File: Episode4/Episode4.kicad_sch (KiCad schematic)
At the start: 16 parts, among them J1 BUS 1, J2 BUS 2, J3 BUS 3, J4 BUS 4, J5 BUS 5, J6 BUS 6, J7 BUS 7, J8 Conn_02x31_Top_Bottom, J9 Conn_02x18_Top_Bottom

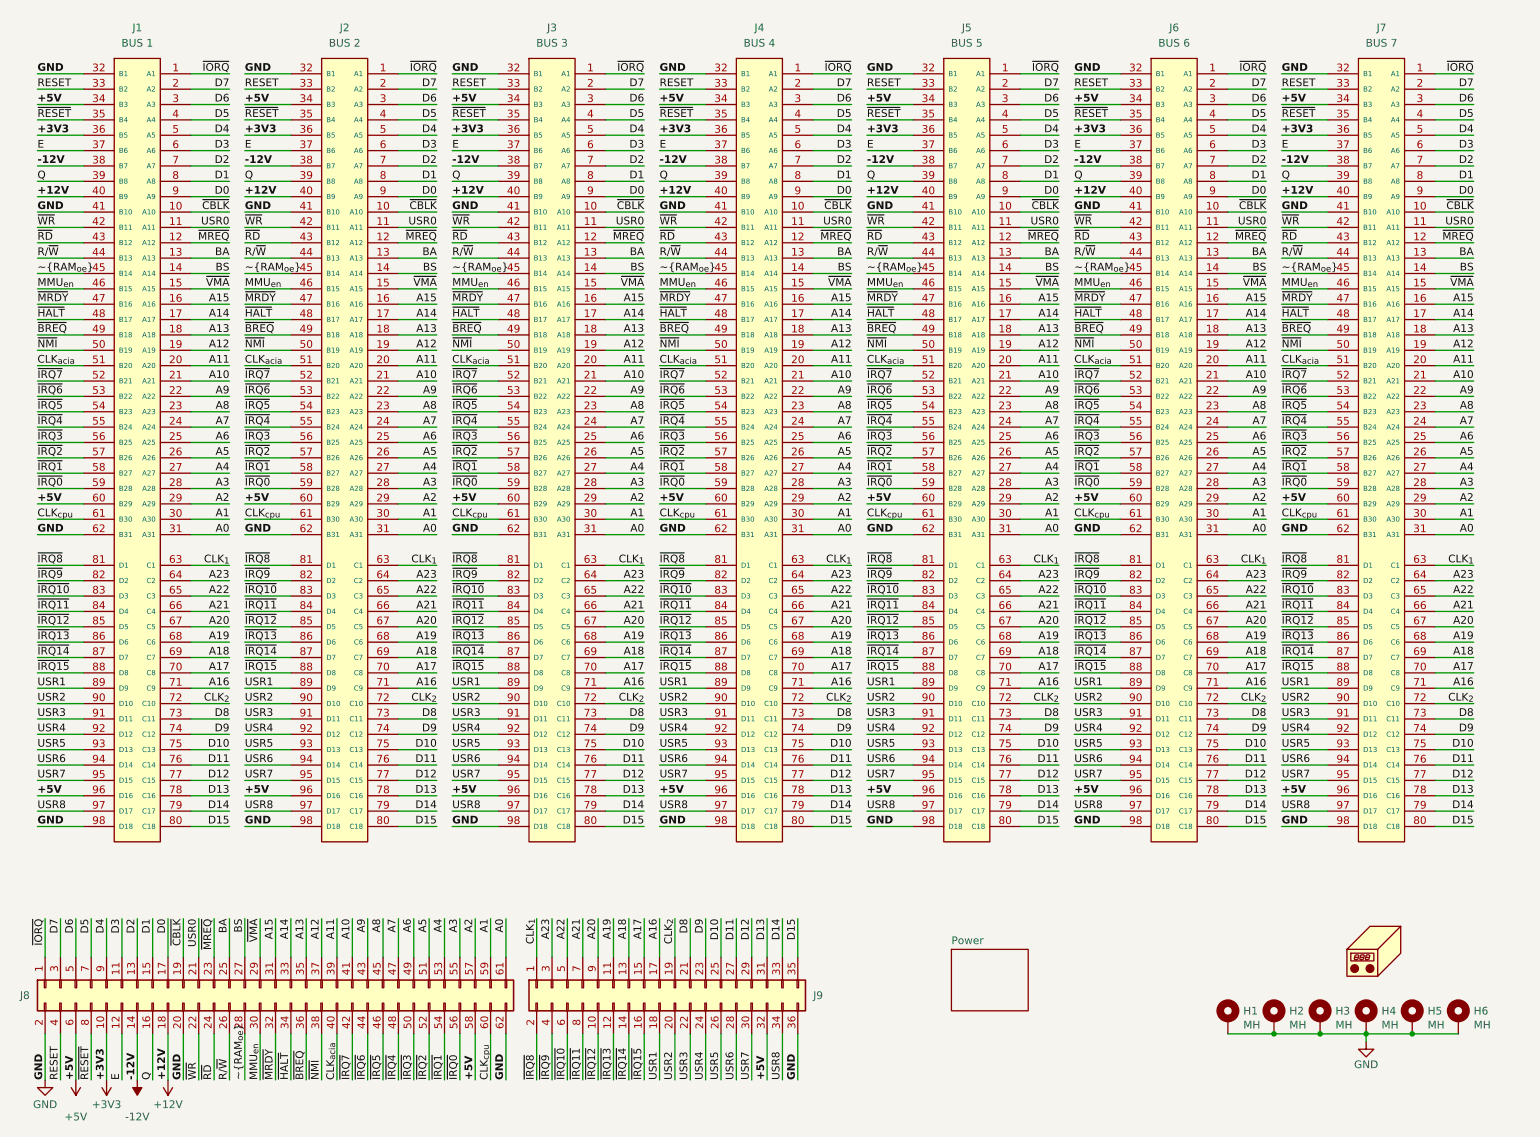
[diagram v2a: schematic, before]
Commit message: Added more capacitors and extended the bus form 7 to 12
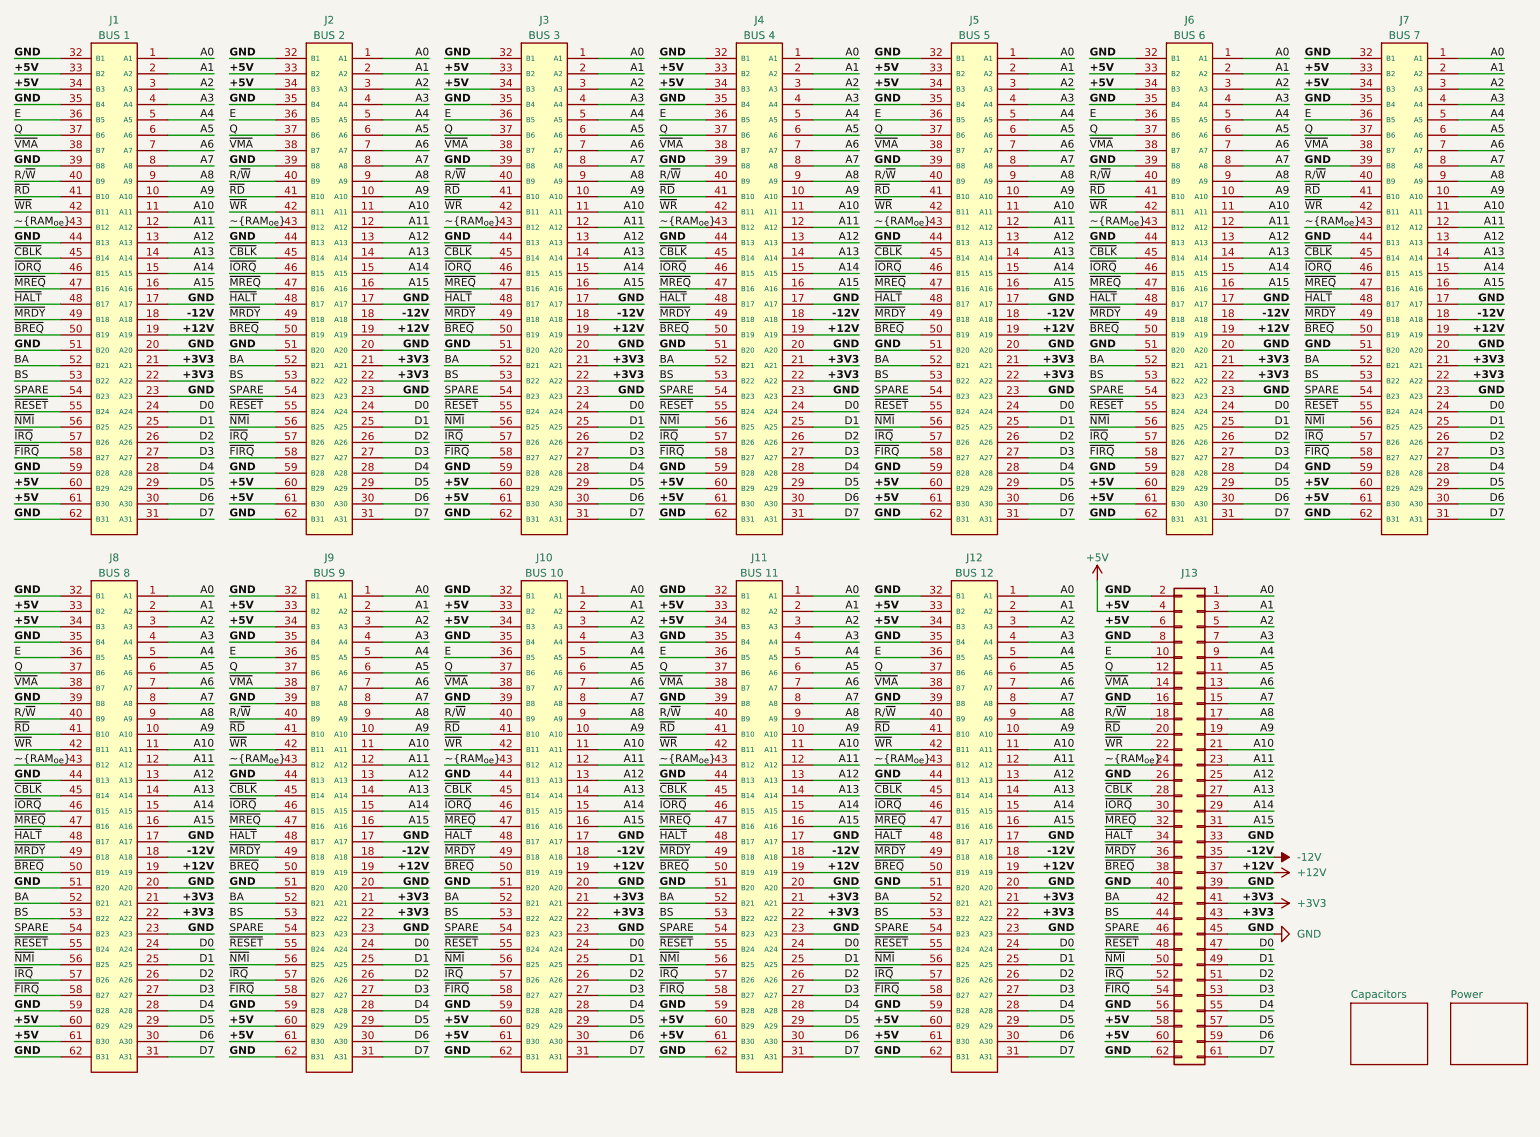
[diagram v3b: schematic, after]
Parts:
- removed H1, H2, H3, H4, H5, H6: MH, MountingHole:MountingHole_3.5mm_Pad_Via, symbol Mechanical:MountingHole_Pad
- removed J1: BUS 1, MicroHobbyist:ISA_Connector_98, symbol MicroHobbyist:ISA_CARD_CONNECTOR_16BIT
- removed J2: BUS 2, MicroHobbyist:ISA_Connector_98, symbol MicroHobbyist:ISA_CARD_CONNECTOR_16BIT
- removed J3: BUS 3, MicroHobbyist:ISA_Connector_98, symbol MicroHobbyist:ISA_CARD_CONNECTOR_16BIT
- removed J4: BUS 4, MicroHobbyist:ISA_Connector_98, symbol MicroHobbyist:ISA_CARD_CONNECTOR_16BIT
- removed J5: BUS 5, MicroHobbyist:ISA_Connector_98, symbol MicroHobbyist:ISA_CARD_CONNECTOR_16BIT
- removed J6: BUS 6, MicroHobbyist:ISA_Connector_98, symbol MicroHobbyist:ISA_CARD_CONNECTOR_16BIT
- removed J7: BUS 7, MicroHobbyist:ISA_Connector_98, symbol MicroHobbyist:ISA_CARD_CONNECTOR_16BIT
- removed J9: Conn_02x18_Top_Bottom, Connector_PinSocket_2.54mm:PinSocket_2x18_P2.54mm_Vertical, symbol Connector_Generic:Conn_02x18_Odd_Even
- removed N1: Housing, MicroHobbyist:ATX_Backplane, symbol Mechanical:Housing
- added J1: BUS 1, MicroHobbyist:ISA_Connector, symbol MicroHobbyist:ISA_CARD_CONNECTOR_8BIT
- added J10: BUS 10, MicroHobbyist:ISA_Connector, symbol MicroHobbyist:ISA_CARD_CONNECTOR_8BIT
- added J11: BUS 11, MicroHobbyist:ISA_Connector, symbol MicroHobbyist:ISA_CARD_CONNECTOR_8BIT
- added J12: BUS 12, MicroHobbyist:ISA_Connector, symbol MicroHobbyist:ISA_CARD_CONNECTOR_8BIT
- added J2: BUS 2, MicroHobbyist:ISA_Connector, symbol MicroHobbyist:ISA_CARD_CONNECTOR_8BIT
- added J3: BUS 3, MicroHobbyist:ISA_Connector, symbol MicroHobbyist:ISA_CARD_CONNECTOR_8BIT
- added J4: BUS 4, MicroHobbyist:ISA_Connector, symbol MicroHobbyist:ISA_CARD_CONNECTOR_8BIT
- added J5: BUS 5, MicroHobbyist:ISA_Connector, symbol MicroHobbyist:ISA_CARD_CONNECTOR_8BIT
- added J6: BUS 6, MicroHobbyist:ISA_Connector, symbol MicroHobbyist:ISA_CARD_CONNECTOR_8BIT
- added J7: BUS 7, MicroHobbyist:ISA_Connector, symbol MicroHobbyist:ISA_CARD_CONNECTOR_8BIT
- added J8: BUS 8, MicroHobbyist:ISA_Connector, symbol MicroHobbyist:ISA_CARD_CONNECTOR_8BIT
- added J9: BUS 9, MicroHobbyist:ISA_Connector, symbol MicroHobbyist:ISA_CARD_CONNECTOR_8BIT
- renumbered J8 to J13
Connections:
- net CLK_{acia} is gone; now on net GND: J13.40 (Pin_40)
- net CLK_{cpu} is gone; now on net +5V: J13.60 (Pin_60)
- net MMU_{en} is gone; now on net ~{IORQ}: J13.30 (Pin_30)
- net RESET is gone; now on net +5V: J13.4 (Pin_4)
- net USR0 is gone; now on net A10: J13.21 (Pin_21)
- net ~{IRQ0} is gone; now on net GND: J13.56 (Pin_56)
- net ~{IRQ3} is gone; now on net ~{NMI}: J13.50 (Pin_50)
- net ~{IRQ4} is gone; now on net ~{RESET}: J13.48 (Pin_48)
- net ~{IRQ6} is gone; now on net BS: J13.44 (Pin_44)
- net ~{IRQ7} is gone; now on net BA: J13.42 (Pin_42)
- net +12V: now also J13.37 (Pin_37), J1.19 (A19), J10.19 (A19), J11.19 (A19), J12.19 (A19), J2.19 (A19), J3.19 (A19), J4.19 (A19), J5.19 (A19), J6.19 (A19), J7.19 (A19), J8.19 (A19), J9.19 (A19); no longer J13.18 (Pin_18)
- net +3V3: now also J13.41 (Pin_41), J13.43 (Pin_43), J1.21 (A21), J1.22 (A22), J10.21 (A21), J10.22 (A22), J11.21 (A21), J11.22 (A22), J12.21 (A21), J12.22 (A22), J2.21 (A21), J2.22 (A22), J3.21 (A21), J3.22 (A22), J4.21 (A21), J4.22 (A22), J5.21 (A21), J5.22 (A22), J6.21 (A21), J6.22 (A22), J7.21 (A21), J7.22 (A22), J8.21 (A21), J8.22 (A22), J9.21 (A21), J9.22 (A22); no longer J13.10 (Pin_10)
- net +5V: now also J1.33 (B2), J1.34 (B3), J1.60 (B29), J1.61 (B30), J10.33 (B2), J10.34 (B3), J10.60 (B29), J10.61 (B30), J11.33 (B2), J11.34 (B3), J11.60 (B29), J11.61 (B30), J12.33 (B2), J12.34 (B3), J12.60 (B29), J12.61 (B30), J2.33 (B2), J2.34 (B3), J2.60 (B29), J2.61 (B30), J3.33 (B2), J3.34 (B3), J3.60 (B29), J3.61 (B30), J4.33 (B2), J4.34 (B3), J4.60 (B29), J4.61 (B30), J5.33 (B2), J5.34 (B3), J5.60 (B29), J5.61 (B30), J6.33 (B2), J6.34 (B3), J6.60 (B29), J6.61 (B30), J7.33 (B2), J7.34 (B3), J7.60 (B29), J7.61 (B30), J8.33 (B2), J8.34 (B3), J8.60 (B29), J8.61 (B30), J9.33 (B2), J9.34 (B3), J9.60 (B29), J9.61 (B30)
- net -12V: now also J13.35 (Pin_35), J1.18 (A18), J10.18 (A18), J11.18 (A18), J12.18 (A18), J2.18 (A18), J3.18 (A18), J4.18 (A18), J5.18 (A18), J6.18 (A18), J7.18 (A18), J8.18 (A18), J9.18 (A18); no longer J13.14 (Pin_14)
- net A0: now also J13.1 (Pin_1), J1.1 (A1), J10.1 (A1), J11.1 (A1), J12.1 (A1), J2.1 (A1), J3.1 (A1), J4.1 (A1), J5.1 (A1), J6.1 (A1), J7.1 (A1), J8.1 (A1), J9.1 (A1); no longer J13.61 (Pin_61)
- net A1: now also J13.3 (Pin_3), J1.2 (A2), J10.2 (A2), J11.2 (A2), J12.2 (A2), J2.2 (A2), J3.2 (A2), J4.2 (A2), J5.2 (A2), J6.2 (A2), J7.2 (A2), J8.2 (A2), J9.2 (A2); no longer J13.59 (Pin_59)
- net A10: now also J1.11 (A11), J10.11 (A11), J11.11 (A11), J12.11 (A11), J2.11 (A11), J3.11 (A11), J4.11 (A11), J5.11 (A11), J6.11 (A11), J7.11 (A11), J8.11 (A11), J9.11 (A11); no longer J13.41 (Pin_41)
- net A11: now also J13.23 (Pin_23), J1.12 (A12), J10.12 (A12), J11.12 (A12), J12.12 (A12), J2.12 (A12), J3.12 (A12), J4.12 (A12), J5.12 (A12), J6.12 (A12), J7.12 (A12), J8.12 (A12), J9.12 (A12); no longer J13.39 (Pin_39)
- net A12: now also J13.25 (Pin_25), J1.13 (A13), J10.13 (A13), J11.13 (A13), J12.13 (A13), J2.13 (A13), J3.13 (A13), J4.13 (A13), J5.13 (A13), J6.13 (A13), J7.13 (A13), J8.13 (A13), J9.13 (A13); no longer J13.37 (Pin_37)
- net A13: now also J13.27 (Pin_27), J1.14 (A14), J10.14 (A14), J11.14 (A14), J12.14 (A14), J2.14 (A14), J3.14 (A14), J4.14 (A14), J5.14 (A14), J6.14 (A14), J7.14 (A14), J8.14 (A14), J9.14 (A14); no longer J13.35 (Pin_35)
- net A14: now also J13.29 (Pin_29), J1.15 (A15), J10.15 (A15), J11.15 (A15), J12.15 (A15), J2.15 (A15), J3.15 (A15), J4.15 (A15), J5.15 (A15), J6.15 (A15), J7.15 (A15), J8.15 (A15), J9.15 (A15); no longer J13.33 (Pin_33)
- net A15: now also J1.16 (A16), J10.16 (A16), J11.16 (A16), J12.16 (A16), J2.16 (A16), J3.16 (A16), J4.16 (A16), J5.16 (A16), J6.16 (A16), J7.16 (A16), J8.16 (A16), J9.16 (A16)
- net A2: now also J13.5 (Pin_5), J1.3 (A3), J10.3 (A3), J11.3 (A3), J12.3 (A3), J2.3 (A3), J3.3 (A3), J4.3 (A3), J5.3 (A3), J6.3 (A3), J7.3 (A3), J8.3 (A3), J9.3 (A3); no longer J13.57 (Pin_57)
- net A3: now also J13.7 (Pin_7), J1.4 (A4), J10.4 (A4), J11.4 (A4), J12.4 (A4), J2.4 (A4), J3.4 (A4), J4.4 (A4), J5.4 (A4), J6.4 (A4), J7.4 (A4), J8.4 (A4), J9.4 (A4); no longer J13.55 (Pin_55)
- net A4: now also J13.9 (Pin_9), J1.5 (A5), J10.5 (A5), J11.5 (A5), J12.5 (A5), J2.5 (A5), J3.5 (A5), J4.5 (A5), J5.5 (A5), J6.5 (A5), J7.5 (A5), J8.5 (A5), J9.5 (A5); no longer J13.53 (Pin_53)
- net A5: now also J13.11 (Pin_11), J1.6 (A6), J10.6 (A6), J11.6 (A6), J12.6 (A6), J2.6 (A6), J3.6 (A6), J4.6 (A6), J5.6 (A6), J6.6 (A6), J7.6 (A6), J8.6 (A6), J9.6 (A6); no longer J13.51 (Pin_51)
- net A6: now also J13.13 (Pin_13), J1.7 (A7), J10.7 (A7), J11.7 (A7), J12.7 (A7), J2.7 (A7), J3.7 (A7), J4.7 (A7), J5.7 (A7), J6.7 (A7), J7.7 (A7), J8.7 (A7), J9.7 (A7); no longer J13.49 (Pin_49)
- net A7: now also J13.15 (Pin_15), J1.8 (A8), J10.8 (A8), J11.8 (A8), J12.8 (A8), J2.8 (A8), J3.8 (A8), J4.8 (A8), J5.8 (A8), J6.8 (A8), J7.8 (A8), J8.8 (A8), J9.8 (A8); no longer J13.47 (Pin_47)
- net A8: now also J13.17 (Pin_17), J1.9 (A9), J10.9 (A9), J11.9 (A9), J12.9 (A9), J2.9 (A9), J3.9 (A9), J4.9 (A9), J5.9 (A9), J6.9 (A9), J7.9 (A9), J8.9 (A9), J9.9 (A9); no longer J13.45 (Pin_45)
- net A9: now also J13.19 (Pin_19), J1.10 (A10), J10.10 (A10), J11.10 (A10), J12.10 (A10), J2.10 (A10), J3.10 (A10), J4.10 (A10), J5.10 (A10), J6.10 (A10), J7.10 (A10), J8.10 (A10), J9.10 (A10); no longer J13.43 (Pin_43)
- net BA: now also J1.52 (B21), J10.52 (B21), J11.52 (B21), J12.52 (B21), J2.52 (B21), J3.52 (B21), J4.52 (B21), J5.52 (B21), J6.52 (B21), J7.52 (B21), J8.52 (B21), J9.52 (B21); no longer J13.25 (Pin_25)
- net BS: now also J1.53 (B22), J10.53 (B22), J11.53 (B22), J12.53 (B22), J2.53 (B22), J3.53 (B22), J4.53 (B22), J5.53 (B22), J6.53 (B22), J7.53 (B22), J8.53 (B22), J9.53 (B22); no longer J13.27 (Pin_27)
- net D0: now also J13.47 (Pin_47), J1.24 (A24), J10.24 (A24), J11.24 (A24), J12.24 (A24), J2.24 (A24), J3.24 (A24), J4.24 (A24), J5.24 (A24), J6.24 (A24), J7.24 (A24), J8.24 (A24), J9.24 (A24); no longer J13.17 (Pin_17)
- net D1: now also J13.49 (Pin_49), J1.25 (A25), J10.25 (A25), J11.25 (A25), J12.25 (A25), J2.25 (A25), J3.25 (A25), J4.25 (A25), J5.25 (A25), J6.25 (A25), J7.25 (A25), J8.25 (A25), J9.25 (A25); no longer J13.15 (Pin_15)
- net D2: now also J13.51 (Pin_51), J1.26 (A26), J10.26 (A26), J11.26 (A26), J12.26 (A26), J2.26 (A26), J3.26 (A26), J4.26 (A26), J5.26 (A26), J6.26 (A26), J7.26 (A26), J8.26 (A26), J9.26 (A26); no longer J13.13 (Pin_13)
- net D3: now also J13.53 (Pin_53), J1.27 (A27), J10.27 (A27), J11.27 (A27), J12.27 (A27), J2.27 (A27), J3.27 (A27), J4.27 (A27), J5.27 (A27), J6.27 (A27), J7.27 (A27), J8.27 (A27), J9.27 (A27); no longer J13.11 (Pin_11)
- net D4: now also J13.55 (Pin_55), J1.28 (A28), J10.28 (A28), J11.28 (A28), J12.28 (A28), J2.28 (A28), J3.28 (A28), J4.28 (A28), J5.28 (A28), J6.28 (A28), J7.28 (A28), J8.28 (A28), J9.28 (A28); no longer J13.9 (Pin_9)
- net D5: now also J13.57 (Pin_57), J1.29 (A29), J10.29 (A29), J11.29 (A29), J12.29 (A29), J2.29 (A29), J3.29 (A29), J4.29 (A29), J5.29 (A29), J6.29 (A29), J7.29 (A29), J8.29 (A29), J9.29 (A29); no longer J13.7 (Pin_7)
- net D6: now also J13.59 (Pin_59), J1.30 (A30), J10.30 (A30), J11.30 (A30), J12.30 (A30), J2.30 (A30), J3.30 (A30), J4.30 (A30), J5.30 (A30), J6.30 (A30), J7.30 (A30), J8.30 (A30), J9.30 (A30); no longer J13.5 (Pin_5)
- net D7: now also J13.61 (Pin_61), J1.31 (A31), J10.31 (A31), J11.31 (A31), J12.31 (A31), J2.31 (A31), J3.31 (A31), J4.31 (A31), J5.31 (A31), J6.31 (A31), J7.31 (A31), J8.31 (A31), J9.31 (A31); no longer J13.3 (Pin_3)
- net E: now also J13.10 (Pin_10), J1.36 (B5), J10.36 (B5), J11.36 (B5), J12.36 (B5), J2.36 (B5), J3.36 (B5), J4.36 (B5), J5.36 (B5), J6.36 (B5), J7.36 (B5), J8.36 (B5), J9.36 (B5); no longer J13.12 (Pin_12)
- net GND: now also J13.16 (Pin_16), J13.26 (Pin_26), J13.33 (Pin_33), J13.39 (Pin_39), J13.45 (Pin_45), J13.8 (Pin_8), J1.17 (A17), J1.20 (A20), J1.23 (A23), J1.32 (B1), J1.35 (B4), J1.39 (B8), J1.44 (B13), J1.51 (B20), J1.59 (B28), J1.62 (B31), J10.17 (A17), J10.20 (A20), J10.23 (A23), J10.32 (B1), J10.35 (B4), J10.39 (B8), J10.44 (B13), J10.51 (B20), J10.59 (B28), J10.62 (B31), J11.17 (A17), J11.20 (A20), J11.23 (A23), J11.32 (B1), J11.35 (B4), J11.39 (B8), J11.44 (B13), J11.51 (B20), J11.59 (B28), J11.62 (B31), J12.17 (A17), J12.20 (A20), J12.23 (A23), J12.32 (B1), J12.35 (B4), J12.39 (B8), J12.44 (B13), J12.51 (B20), J12.59 (B28), J12.62 (B31), J2.17 (A17), J2.20 (A20), J2.23 (A23), J2.32 (B1), J2.35 (B4), J2.39 (B8), J2.44 (B13), J2.51 (B20), J2.59 (B28), J2.62 (B31), J3.17 (A17), J3.20 (A20), J3.23 (A23), J3.32 (B1), J3.35 (B4), J3.39 (B8), J3.44 (B13), J3.51 (B20), J3.59 (B28), J3.62 (B31), J4.17 (A17), J4.20 (A20), J4.23 (A23), J4.32 (B1), J4.35 (B4), J4.39 (B8), J4.44 (B13), J4.51 (B20), J4.59 (B28), J4.62 (B31), J5.17 (A17), J5.20 (A20), J5.23 (A23), J5.32 (B1), J5.35 (B4), J5.39 (B8), J5.44 (B13), J5.51 (B20), J5.59 (B28), J5.62 (B31), J6.17 (A17), J6.20 (A20), J6.23 (A23), J6.32 (B1), J6.35 (B4), J6.39 (B8), J6.44 (B13), J6.51 (B20), J6.59 (B28), J6.62 (B31), J7.17 (A17), J7.20 (A20), J7.23 (A23), J7.32 (B1), J7.35 (B4), J7.39 (B8), J7.44 (B13), J7.51 (B20), J7.59 (B28), J7.62 (B31), J8.17 (A17), J8.20 (A20), J8.23 (A23), J8.32 (B1), J8.35 (B4), J8.39 (B8), J8.44 (B13), J8.51 (B20), J8.59 (B28), J8.62 (B31), J9.17 (A17), J9.20 (A20), J9.23 (A23), J9.32 (B1), J9.35 (B4), J9.39 (B8), J9.44 (B13), J9.51 (B20), J9.59 (B28), J9.62 (B31); no longer J13.20 (Pin_20)
- net Q: now also J13.12 (Pin_12), J1.37 (B6), J10.37 (B6), J11.37 (B6), J12.37 (B6), J2.37 (B6), J3.37 (B6), J4.37 (B6), J5.37 (B6), J6.37 (B6), J7.37 (B6), J8.37 (B6), J9.37 (B6); no longer J13.16 (Pin_16)
- net R/~{W}: now also J13.18 (Pin_18), J1.40 (B9), J10.40 (B9), J11.40 (B9), J12.40 (B9), J2.40 (B9), J3.40 (B9), J4.40 (B9), J5.40 (B9), J6.40 (B9), J7.40 (B9), J8.40 (B9), J9.40 (B9); no longer J13.26 (Pin_26)
- net ~{BREQ}: now also J13.38 (Pin_38), J1.50 (B19), J10.50 (B19), J11.50 (B19), J12.50 (B19), J2.50 (B19), J3.50 (B19), J4.50 (B19), J5.50 (B19), J6.50 (B19), J7.50 (B19), J8.50 (B19), J9.50 (B19); no longer J13.36 (Pin_36)
- net ~{CBLK}: now also J13.28 (Pin_28), J1.45 (B14), J10.45 (B14), J11.45 (B14), J12.45 (B14), J2.45 (B14), J3.45 (B14), J4.45 (B14), J5.45 (B14), J6.45 (B14), J7.45 (B14), J8.45 (B14), J9.45 (B14); no longer J13.19 (Pin_19)
- net ~{HALT}: now also J1.48 (B17), J10.48 (B17), J11.48 (B17), J12.48 (B17), J2.48 (B17), J3.48 (B17), J4.48 (B17), J5.48 (B17), J6.48 (B17), J7.48 (B17), J8.48 (B17), J9.48 (B17)
- net ~{IORQ}: now also J1.46 (B15), J10.46 (B15), J11.46 (B15), J12.46 (B15), J2.46 (B15), J3.46 (B15), J4.46 (B15), J5.46 (B15), J6.46 (B15), J7.46 (B15), J8.46 (B15), J9.46 (B15); no longer J13.1 (Pin_1)
- net ~{MRDY}: now also J13.36 (Pin_36), J1.49 (B18), J10.49 (B18), J11.49 (B18), J12.49 (B18), J2.49 (B18), J3.49 (B18), J4.49 (B18), J5.49 (B18), J6.49 (B18), J7.49 (B18), J8.49 (B18), J9.49 (B18); no longer J13.32 (Pin_32)
- net ~{MREQ}: now also J13.32 (Pin_32), J1.47 (B16), J10.47 (B16), J11.47 (B16), J12.47 (B16), J2.47 (B16), J3.47 (B16), J4.47 (B16), J5.47 (B16), J6.47 (B16), J7.47 (B16), J8.47 (B16), J9.47 (B16); no longer J13.23 (Pin_23)
- net ~{NMI}: now also J1.56 (B25), J10.56 (B25), J11.56 (B25), J12.56 (B25), J2.56 (B25), J3.56 (B25), J4.56 (B25), J5.56 (B25), J6.56 (B25), J7.56 (B25), J8.56 (B25), J9.56 (B25); no longer J13.38 (Pin_38)
- net ~{RAM_{oe}}: now also J13.24 (Pin_24), J1.43 (B12), J10.43 (B12), J11.43 (B12), J12.43 (B12), J2.43 (B12), J3.43 (B12), J4.43 (B12), J5.43 (B12), J6.43 (B12), J7.43 (B12), J8.43 (B12), J9.43 (B12); no longer J13.28 (Pin_28)
- net ~{RD}: now also J13.20 (Pin_20), J1.41 (B10), J10.41 (B10), J11.41 (B10), J12.41 (B10), J2.41 (B10), J3.41 (B10), J4.41 (B10), J5.41 (B10), J6.41 (B10), J7.41 (B10), J8.41 (B10), J9.41 (B10); no longer J13.24 (Pin_24)
- net ~{RESET}: now also J1.55 (B24), J10.55 (B24), J11.55 (B24), J12.55 (B24), J2.55 (B24), J3.55 (B24), J4.55 (B24), J5.55 (B24), J6.55 (B24), J7.55 (B24), J8.55 (B24), J9.55 (B24); no longer J13.8 (Pin_8)
- net ~{VMA}: now also J13.14 (Pin_14), J1.38 (B7), J10.38 (B7), J11.38 (B7), J12.38 (B7), J2.38 (B7), J3.38 (B7), J4.38 (B7), J5.38 (B7), J6.38 (B7), J7.38 (B7), J8.38 (B7), J9.38 (B7); no longer J13.29 (Pin_29)
- net ~{WR}: now also J1.42 (B11), J10.42 (B11), J11.42 (B11), J12.42 (B11), J2.42 (B11), J3.42 (B11), J4.42 (B11), J5.42 (B11), J6.42 (B11), J7.42 (B11), J8.42 (B11), J9.42 (B11)
- net ~{IRQ1} renamed ~{FIRQ}
- net ~{FIRQ}: now also J1.58 (B27), J10.58 (B27), J11.58 (B27), J12.58 (B27), J2.58 (B27), J3.58 (B27), J4.58 (B27), J5.58 (B27), J6.58 (B27), J7.58 (B27), J8.58 (B27), J9.58 (B27)
- net ~{IRQ2} renamed ~{IRQ}
- net ~{IRQ}: now also J1.57 (B26), J10.57 (B26), J11.57 (B26), J12.57 (B26), J2.57 (B26), J3.57 (B26), J4.57 (B26), J5.57 (B26), J6.57 (B26), J7.57 (B26), J8.57 (B26), J9.57 (B26)
- net ~{IRQ5} renamed SPARE
- net SPARE: now also J1.54 (B23), J10.54 (B23), J11.54 (B23), J12.54 (B23), J2.54 (B23), J3.54 (B23), J4.54 (B23), J5.54 (B23), J6.54 (B23), J7.54 (B23), J8.54 (B23), J9.54 (B23)
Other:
- added sheet Capacitors (Caps.kicad_sch)
- title: 16-bit ATX backblane -> 8-bit ISA style ATX backblane
- moved on the sheet: J13

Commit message: Worked on BOM
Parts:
- J13: value Conn_02x31_Top_Bottom -> BB Con; footprint Connector_PinSocket_2.54mm:PinSocket_2x31_P2.54mm_Vertical -> Connector_PinSocket_2.54mm:PinSocket_2x32_P2.54mm_Vertical; Manufacturer_Name (none) -> 3M Electronic Solutions Division; Manufacturer_Part_Number (none) -> 929852-01-16-RA
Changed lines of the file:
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@@
 			)
 		)
-		(property "Value" "Conn_02x31_Top_Bottom"
+		(property "Value" "BB Con"
 			(at 209.5501 106.68 90)
 			(effects
@@
 			)
 		)
-		(property "Footprint" "Connector_PinSocket_2.54mm:PinSocket_2x31_P2.54mm_Vertical"
+		(property "Footprint" "Connector_PinSocket_2.54mm:PinSocket_2x32_P2.54mm_Vertical"
 			(at 212.09 147.32 0)
 			(effects
@@
 			)
 		)
-		(property "Datasheet" "~"
+		(property "Datasheet" "https://multimedia.3m.com/mws/media/22500O/3m-tm-boardmount-skt-100-100-x-100-strt-sldr-tails-ts0815.pdf"
 			(at 212.09 147.32 0)
 			(effects
@@
 			)
 		)
-		(property "Description" "Generic connector, double row, 02x31, odd/even pin numbering scheme (row 1 odd numbers, row 2 even numbers), script generated (kicad-library-utils/schlib/autogen/connector/)"
+		(property "Description" "Headers & Wire Housings 32P STRT BRD MNT SKT 2 ROW 10MICRO\" AU"
 			(at 212.09 147.32 0)
 			(effects
+				(font
+					(size 1.27 1.27)
+				)
+				(hide yes)
+			)
+		)
+		(property "Manufacturer_Name" "3M Electronic Solutions Division"
+			(at 212.09 147.32 0)
+			(effects
+				(font
+					(size 1.27 1.27)
+				)
+				(hide yes)
+			)
+		)
+		(property "Manufacturer_Part_Number" "929852-01-16-RA"
+			(at 212.09 147.32 0)
+			(effects

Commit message: Changed bus from 62 to 72 pins
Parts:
- added C1, C2: 1µF, Capacitor_SMD:C_0805_2012Metric_Pad1.18x1.45mm_HandSolder, symbol Device:C
- added D1, D5: TVS 5V, Diode_SMD:D_SMB, symbol Diode:SM6T6V8A
- added D2, D6: TVS 3V3, Diode_SMD:D_SMB, symbol Diode:SM6T6V8A
- added D3, D4, D7, D8: TVS 12V, Diode_SMD:D_SMB, symbol Diode:SM6T6V8A
- added H1, H10, H2, H3, H4, H5, H6, H7, H8, H9: MH, MountingHole:MountingHole_3.5mm_Pad_Via, symbol Mechanical:MountingHole_Pad
- added J8: ATX POWER, MicroHobbyist:ATX_PSU_CONN, symbol 0_Library:ATX_PSU_CONN
- added R1: 10K, Resistor_SMD:R_0805_2012Metric_Pad1.20x1.40mm_HandSolder, symbol Device:R_US
- added R2: 1K, Resistor_SMD:R_0805_2012Metric_Pad1.20x1.40mm_HandSolder, symbol Device:R_US
- added R3: 330, Resistor_SMD:R_0805_2012Metric_Pad1.20x1.40mm_HandSolder, symbol Device:R_US
- added R4: 20K, Resistor_SMD:R_0805_2012Metric_Pad1.20x1.40mm_HandSolder, symbol Device:R_US
- added SW1: POWER, MicroHobbyist:TS2912121G300D, symbol MicroHobbyist:LED Tack PushButton
- added U1: 74HCT14, Package_SO:SOIC-14_3.9x8.7mm_P1.27mm, symbol 74xx:74HC14
- added U2: 74HCT74, Package_SO:SOIC-14_3.9x8.7mm_P1.27mm, symbol 74xx:74HC74
- J1: value BUS 1 -> CARD; footprint MicroHobbyist:ISA_Connector -> MicroHobbyist:72-pin CE connector; symbol MicroHobbyist:ISA_CARD_CONNECTOR_8BIT -> MicroHobbyist:72-pin Card Edge (ISA style); Manufacturer_Part_Number 6-5530843-5 -> 5530843-8; Mouser Part Number 571-6-5530843-5 -> 571-5530843-8; Mouser Price/Stock https://www.mouser.co.uk/ProductDetail/TE-Connectivity/6-55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 -> https://www.mouser.co.uk/ProductDetail/TE-Connectivity/5530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
- J10: renamed from J8; value BUS 8 -> CARD; footprint MicroHobbyist:ISA_Connector -> MicroHobbyist:72-pin CE connector; symbol MicroHobbyist:ISA_CARD_CONNECTOR_8BIT -> MicroHobbyist:72-pin Card Edge (ISA style); Manufacturer_Part_Number 6-5530843-5 -> 5530843-8; Mouser Part Number 571-6-5530843-5 -> 571-5530843-8; Mouser Price/Stock https://www.mouser.co.uk/ProductDetail/TE-Connectivity/6-55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 -> https://www.mouser.co.uk/ProductDetail/TE-Connectivity/5530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
- J11: renamed from J9; value BUS 9 -> CARD; footprint MicroHobbyist:ISA_Connector -> MicroHobbyist:72-pin CE connector; symbol MicroHobbyist:ISA_CARD_CONNECTOR_8BIT -> MicroHobbyist:72-pin Card Edge (ISA style); Manufacturer_Part_Number 6-5530843-5 -> 5530843-8; Mouser Part Number 571-6-5530843-5 -> 571-5530843-8; Mouser Price/Stock https://www.mouser.co.uk/ProductDetail/TE-Connectivity/6-55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 -> https://www.mouser.co.uk/ProductDetail/TE-Connectivity/5530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
- J12: renamed from J10; value BUS 10 -> CARD; footprint MicroHobbyist:ISA_Connector -> MicroHobbyist:72-pin CE connector; symbol MicroHobbyist:ISA_CARD_CONNECTOR_8BIT -> MicroHobbyist:72-pin Card Edge (ISA style); Manufacturer_Part_Number 6-5530843-5 -> 5530843-8; Mouser Part Number 571-6-5530843-5 -> 571-5530843-8; Mouser Price/Stock https://www.mouser.co.uk/ProductDetail/TE-Connectivity/6-55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 -> https://www.mouser.co.uk/ProductDetail/TE-Connectivity/5530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
- J13: renamed from J11; value BUS 11 -> CARD; footprint MicroHobbyist:ISA_Connector -> MicroHobbyist:72-pin CE connector; symbol MicroHobbyist:ISA_CARD_CONNECTOR_8BIT -> MicroHobbyist:72-pin Card Edge (ISA style); Manufacturer_Part_Number 6-5530843-5 -> 5530843-8; Mouser Part Number 571-6-5530843-5 -> 571-5530843-8; Mouser Price/Stock https://www.mouser.co.uk/ProductDetail/TE-Connectivity/6-55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 -> https://www.mouser.co.uk/ProductDetail/TE-Connectivity/5530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
- J14: renamed from J12; value BUS 12 -> CARD; footprint MicroHobbyist:ISA_Connector -> MicroHobbyist:72-pin CE connector; symbol MicroHobbyist:ISA_CARD_CONNECTOR_8BIT -> MicroHobbyist:72-pin Card Edge (ISA style); Manufacturer_Part_Number 6-5530843-5 -> 5530843-8; Mouser Part Number 571-6-5530843-5 -> 571-5530843-8; Mouser Price/Stock https://www.mouser.co.uk/ProductDetail/TE-Connectivity/6-55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 -> https://www.mouser.co.uk/ProductDetail/TE-Connectivity/5530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
- J2: value BUS 2 -> CARD; footprint MicroHobbyist:ISA_Connector -> MicroHobbyist:72-pin CE connector; symbol MicroHobbyist:ISA_CARD_CONNECTOR_8BIT -> MicroHobbyist:72-pin Card Edge (ISA style); Manufacturer_Part_Number 6-5530843-5 -> 5530843-8; Mouser Part Number 571-6-5530843-5 -> 571-5530843-8; Mouser Price/Stock https://www.mouser.co.uk/ProductDetail/TE-Connectivity/6-55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 -> https://www.mouser.co.uk/ProductDetail/TE-Connectivity/5530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
- J3: value BUS 3 -> CARD; footprint MicroHobbyist:ISA_Connector -> MicroHobbyist:72-pin CE connector; symbol MicroHobbyist:ISA_CARD_CONNECTOR_8BIT -> MicroHobbyist:72-pin Card Edge (ISA style); Manufacturer_Part_Number 6-5530843-5 -> 5530843-8; Mouser Part Number 571-6-5530843-5 -> 571-5530843-8; Mouser Price/Stock https://www.mouser.co.uk/ProductDetail/TE-Connectivity/6-55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 -> https://www.mouser.co.uk/ProductDetail/TE-Connectivity/5530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
- J4: value BUS 4 -> CARD; footprint MicroHobbyist:ISA_Connector -> MicroHobbyist:72-pin CE connector; symbol MicroHobbyist:ISA_CARD_CONNECTOR_8BIT -> MicroHobbyist:72-pin Card Edge (ISA style); Manufacturer_Part_Number 6-5530843-5 -> 5530843-8; Mouser Part Number 571-6-5530843-5 -> 571-5530843-8; Mouser Price/Stock https://www.mouser.co.uk/ProductDetail/TE-Connectivity/6-55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 -> https://www.mouser.co.uk/ProductDetail/TE-Connectivity/5530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
- J5: value BUS 5 -> CARD; footprint MicroHobbyist:ISA_Connector -> MicroHobbyist:72-pin CE connector; symbol MicroHobbyist:ISA_CARD_CONNECTOR_8BIT -> MicroHobbyist:72-pin Card Edge (ISA style); Manufacturer_Part_Number 6-5530843-5 -> 5530843-8; Mouser Part Number 571-6-5530843-5 -> 571-5530843-8; Mouser Price/Stock https://www.mouser.co.uk/ProductDetail/TE-Connectivity/6-55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 -> https://www.mouser.co.uk/ProductDetail/TE-Connectivity/5530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
- J6: value BUS 6 -> CARD; footprint MicroHobbyist:ISA_Connector -> MicroHobbyist:72-pin CE connector; symbol MicroHobbyist:ISA_CARD_CONNECTOR_8BIT -> MicroHobbyist:72-pin Card Edge (ISA style); Manufacturer_Part_Number 6-5530843-5 -> 5530843-8; Mouser Part Number 571-6-5530843-5 -> 571-5530843-8; Mouser Price/Stock https://www.mouser.co.uk/ProductDetail/TE-Connectivity/6-55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 -> https://www.mouser.co.uk/ProductDetail/TE-Connectivity/5530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
- J7: renamed from J13; footprint Connector_PinSocket_2.54mm:PinSocket_2x32_P2.54mm_Vertical -> Connector_PinSocket_2.54mm:PinSocket_2x36_P2.54mm_Vertical; symbol Connector_Generic:Conn_02x31_Odd_Even -> Connector_Generic:Conn_02x36_Odd_Even; Manufacturer_Part_Number 929852-01-16-RA -> 929852-01-36-RA
- J9: renamed from J7; value BUS 7 -> CARD; footprint MicroHobbyist:ISA_Connector -> MicroHobbyist:72-pin CE connector; symbol MicroHobbyist:ISA_CARD_CONNECTOR_8BIT -> MicroHobbyist:72-pin Card Edge (ISA style); Manufacturer_Part_Number 6-5530843-5 -> 5530843-8; Mouser Part Number 571-6-5530843-5 -> 571-5530843-8; Mouser Price/Stock https://www.mouser.co.uk/ProductDetail/TE-Connectivity/6-55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 -> https://www.mouser.co.uk/ProductDetail/TE-Connectivity/5530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
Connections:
- net +12V: now also J1.47 (A24), J10.47 (A24), J11.47 (A24), J12.47 (A24), J13.47 (A24), J14.47 (A24), J2.47 (A24), J3.47 (A24), J4.47 (A24), J5.47 (A24), J6.47 (A24), J7.47 (Pin_47)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; no longer J1.19 (A19), J10.19 (A19), J11.19 (A19), J12.19 (A19), J13.19 (A19), J14.19 (A19), J2.19 (A19), J3.19 (A19), J4.19 (A19), J5.19 (A19), J6.19 (A19), J7.37 (Pin_37)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
- net +3V3: now also J1.43 (A22), J1.44 (B22), J10.43 (A22), J10.44 (B22), J11.43 (A22), J11.44 (B22), J12.43 (A22), J12.44 (B22), J13.43 (A22), J13.44 (B22), J14.43 (A22), J14.44 (B22)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; no longer J1.21 (A21), J1.22 (A22), J10.21 (A21), J10.22 (A22), J11.21 (A21), J11.22 (A22), J12.21 (A21), J12.22 (A22), J13.21 (A21), J13.22 (A22), J14.21 (A21), J14.22 (A22)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
- net +5V: now also J1.1 (A1), J1.2 (B1), J1.71 (A36), J1.72 (B36), J10.1 (A1), J10.2 (B1), J10.71 (A36), J10.72 (B36), J11.1 (A1), J11.2 (B1), J11.71 (A36), J11.72 (B36)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; no longer J1.33 (B2), J1.34 (B3), J1.60 (B29), J1.61 (B30), J10.33 (B2), J10.34 (B3), J10.60 (B29), J10.61 (B30), J11.33 (B2), J11.34 (B3), J11.60 (B29), J11.61 (B30)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
- net -12V: now also J1.49 (A25), J10.49 (A25), J11.49 (A25), J12.49 (A25), J13.49 (A25), J14.49 (A25), J2.49 (A25), J3.49 (A25), J4.49 (A25), J5.49 (A25), J6.49 (A25), J7.49 (Pin_49)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; no longer J1.18 (A18), J10.18 (A18), J11.18 (A18), J12.18 (A18), J13.18 (A18), J14.18 (A18), J2.18 (A18), J3.18 (A18), J4.18 (A18), J5.18 (A18), J6.18 (A18), J7.35 (Pin_35)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
- net A0: now also J1.5 (A3), J10.5 (A3), J11.5 (A3), J12.5 (A3), J13.5 (A3), J14.5 (A3), J2.5 (A3), J3.5 (A3), J4.5 (A3), J5.5 (A3), J6.5 (A3), J7.5 (Pin_5)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; no longer J1.1 (A1), J10.1 (A1), J11.1 (A1), J12.1 (A1), J13.1 (A1), J14.1 (A1), J2.1 (A1), J3.1 (A1), J4.1 (A1), J5.1 (A1), J6.1 (A1), J7.1 (Pin_1)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
- net A1: now also J1.7 (A4), J10.7 (A4), J11.7 (A4), J12.7 (A4), J13.7 (A4), J14.7 (A4), J2.7 (A4), J3.7 (A4), J4.7 (A4), J5.7 (A4), J6.7 (A4), J7.7 (Pin_7)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; no longer J1.2 (A2), J10.2 (A2), J11.2 (A2), J12.2 (A2), J13.2 (A2), J14.2 (A2), J2.2 (A2), J3.2 (A2), J4.2 (A2), J5.2 (A2), J6.2 (A2), J7.3 (Pin_3)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
- net A10: now also J1.27 (A14), J10.27 (A14), J11.27 (A14), J12.27 (A14), J13.27 (A14), J14.27 (A14), J2.27 (A14), J3.27 (A14), J4.27 (A14), J5.27 (A14), J6.27 (A14), J7.27 (Pin_27)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; no longer J1.11 (A11), J10.11 (A11), J11.11 (A11), J12.11 (A11), J13.11 (A11), J14.11 (A11), J2.11 (A11), J3.11 (A11), J4.11 (A11), J5.11 (A11), J6.11 (A11), J7.21 (Pin_21)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
- net A11: now also J1.29 (A15), J10.29 (A15), J11.29 (A15), J12.29 (A15), J13.29 (A15), J14.29 (A15), J2.29 (A15), J3.29 (A15), J4.29 (A15), J5.29 (A15), J6.29 (A15), J7.29 (Pin_29)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; no longer J1.12 (A12), J10.12 (A12), J11.12 (A12), J12.12 (A12), J13.12 (A12), J14.12 (A12), J2.12 (A12), J3.12 (A12), J4.12 (A12), J5.12 (A12), J6.12 (A12), J7.23 (Pin_23)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
- net A12: now also J1.31 (A16), J10.31 (A16), J11.31 (A16), J12.31 (A16), J13.31 (A16), J14.31 (A16), J2.31 (A16), J3.31 (A16), J4.31 (A16), J5.31 (A16), J6.31 (A16), J7.31 (Pin_31)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; no longer J1.13 (A13), J10.13 (A13), J11.13 (A13), J12.13 (A13), J13.13 (A13), J14.13 (A13), J2.13 (A13), J3.13 (A13), J4.13 (A13), J5.13 (A13), J6.13 (A13), J7.25 (Pin_25)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
- net A13: now also J1.33 (A17), J10.33 (A17), J11.33 (A17), J12.33 (A17), J13.33 (A17), J14.33 (A17), J2.33 (A17), J3.33 (A17), J4.33 (A17), J5.33 (A17), J6.33 (A17), J7.33 (Pin_33)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; no longer J1.14 (A14), J10.14 (A14), J11.14 (A14), J12.14 (A14), J13.14 (A14), J14.14 (A14), J2.14 (A14), J3.14 (A14), J4.14 (A14), J5.14 (A14), J6.14 (A14), J7.27 (Pin_27)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
- net A14: now also J1.35 (A18), J10.35 (A18), J11.35 (A18), J12.35 (A18), J13.35 (A18), J14.35 (A18), J2.35 (A18), J3.35 (A18), J4.35 (A18), J5.35 (A18), J6.35 (A18), J7.35 (Pin_35)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; no longer J1.15 (A15), J10.15 (A15), J11.15 (A15), J12.15 (A15), J13.15 (A15), J14.15 (A15), J2.15 (A15), J3.15 (A15), J4.15 (A15), J5.15 (A15), J6.15 (A15), J7.29 (Pin_29)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
- net A15: now also J1.37 (A19), J10.37 (A19), J11.37 (A19), J12.37 (A19), J13.37 (A19), J14.37 (A19), J2.37 (A19), J3.37 (A19), J4.37 (A19), J5.37 (A19), J6.37 (A19), J7.37 (Pin_37)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; no longer J1.16 (A16), J10.16 (A16), J11.16 (A16), J12.16 (A16), J13.16 (A16), J14.16 (A16), J2.16 (A16), J3.16 (A16), J4.16 (A16), J5.16 (A16), J6.16 (A16), J7.31 (Pin_31)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
- net A2: now also J1.9 (A5), J10.9 (A5), J11.9 (A5), J12.9 (A5), J13.9 (A5), J14.9 (A5), J2.9 (A5), J3.9 (A5), J4.9 (A5), J5.9 (A5), J6.9 (A5), J7.9 (Pin_9)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; no longer J1.3 (A3), J10.3 (A3), J11.3 (A3), J12.3 (A3), J13.3 (A3), J14.3 (A3), J2.3 (A3), J3.3 (A3), J4.3 (A3), J5.3 (A3), J6.3 (A3), J7.5 (Pin_5)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
- net A3: now also J1.11 (A6), J10.11 (A6), J11.11 (A6), J12.11 (A6), J13.11 (A6), J14.11 (A6), J2.11 (A6), J3.11 (A6), J4.11 (A6), J5.11 (A6), J6.11 (A6), J7.11 (Pin_11)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; no longer J1.4 (A4), J10.4 (A4), J11.4 (A4), J12.4 (A4), J13.4 (A4), J14.4 (A4), J2.4 (A4), J3.4 (A4), J4.4 (A4), J5.4 (A4), J6.4 (A4), J7.7 (Pin_7)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
- net A4: now also J1.13 (A7), J10.13 (A7), J11.13 (A7), J12.13 (A7), J13.13 (A7), J14.13 (A7), J2.13 (A7), J3.13 (A7), J4.13 (A7), J5.13 (A7), J6.13 (A7), J7.13 (Pin_13)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; no longer J1.5 (A5), J10.5 (A5), J11.5 (A5), J12.5 (A5), J13.5 (A5), J14.5 (A5), J2.5 (A5), J3.5 (A5), J4.5 (A5), J5.5 (A5), J6.5 (A5), J7.9 (Pin_9)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
- net A5: now also J1.15 (A8), J10.15 (A8), J11.15 (A8), J12.15 (A8), J13.15 (A8), J14.15 (A8), J2.15 (A8), J3.15 (A8), J4.15 (A8), J5.15 (A8), J6.15 (A8), J7.15 (Pin_15)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; no longer J1.6 (A6), J10.6 (A6), J11.6 (A6), J12.6 (A6), J13.6 (A6), J14.6 (A6), J2.6 (A6), J3.6 (A6), J4.6 (A6), J5.6 (A6), J6.6 (A6), J7.11 (Pin_11)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
- net A6: now also J1.17 (A9), J10.17 (A9), J11.17 (A9), J12.17 (A9), J13.17 (A9), J14.17 (A9), J2.17 (A9), J3.17 (A9), J4.17 (A9), J5.17 (A9), J6.17 (A9), J7.17 (Pin_17)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; no longer J1.7 (A7), J10.7 (A7), J11.7 (A7), J12.7 (A7), J13.7 (A7), J14.7 (A7), J2.7 (A7), J3.7 (A7), J4.7 (A7), J5.7 (A7), J6.7 (A7), J7.13 (Pin_13)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
- net A7: now also J1.19 (A10), J10.19 (A10), J11.19 (A10), J12.19 (A10), J13.19 (A10), J14.19 (A10), J2.19 (A10), J3.19 (A10), J4.19 (A10), J5.19 (A10), J6.19 (A10), J7.19 (Pin_19)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; no longer J1.8 (A8), J10.8 (A8), J11.8 (A8), J12.8 (A8), J13.8 (A8), J14.8 (A8), J2.8 (A8), J3.8 (A8), J4.8 (A8), J5.8 (A8), J6.8 (A8), J7.15 (Pin_15)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
- net A8: now also J1.23 (A12), J10.23 (A12), J11.23 (A12), J12.23 (A12), J13.23 (A12), J14.23 (A12), J2.23 (A12), J3.23 (A12), J4.23 (A12), J5.23 (A12), J6.23 (A12), J7.23 (Pin_23)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; no longer J1.9 (A9), J10.9 (A9), J11.9 (A9), J12.9 (A9), J13.9 (A9), J14.9 (A9), J2.9 (A9), J3.9 (A9), J4.9 (A9), J5.9 (A9), J6.9 (A9), J7.17 (Pin_17)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
- net A9: now also J1.25 (A13), J10.25 (A13), J11.25 (A13), J12.25 (A13), J13.25 (A13), J14.25 (A13), J2.25 (A13), J3.25 (A13), J4.25 (A13), J5.25 (A13), J6.25 (A13), J7.25 (Pin_25)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; no longer J1.10 (A10), J10.10 (A10), J11.10 (A10), J12.10 (A10), J13.10 (A10), J14.10 (A10), J2.10 (A10), J3.10 (A10), J4.10 (A10), J5.10 (A10), J6.10 (A10), J7.19 (Pin_19)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
- net BA: now also J1.48 (B24), J10.48 (B24), J11.48 (B24), J12.48 (B24), J13.48 (B24), J14.48 (B24), J2.48 (B24), J3.48 (B24), J4.48 (B24), J5.48 (B24), J6.48 (B24), J7.48 (Pin_48)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; no longer J1.52 (B21), J10.52 (B21), J11.52 (B21), J12.52 (B21), J13.52 (B21), J14.52 (B21), J2.52 (B21), J3.52 (B21), J4.52 (B21), J5.52 (B21), J6.52 (B21), J7.42 (Pin_42)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
- net BS: now also J1.50 (B25), J10.50 (B25), J11.50 (B25), J12.50 (B25), J13.50 (B25), J14.50 (B25), J2.50 (B25), J3.50 (B25), J4.50 (B25), J5.50 (B25), J6.50 (B25), J7.50 (Pin_50)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; no longer J1.53 (B22), J10.53 (B22), J11.53 (B22), J12.53 (B22), J13.53 (B22), J14.53 (B22), J2.53 (B22), J3.53 (B22), J4.53 (B22), J5.53 (B22), J6.53 (B22), J7.44 (Pin_44)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
- net D0: now also J1.53 (A27), J10.53 (A27), J11.53 (A27), J12.53 (A27), J13.53 (A27), J14.53 (A27), J2.53 (A27), J3.53 (A27), J4.53 (A27), J5.53 (A27), J6.53 (A27), J7.53 (Pin_53)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; no longer J1.24 (A24), J10.24 (A24), J11.24 (A24), J12.24 (A24), J13.24 (A24), J14.24 (A24), J2.24 (A24), J3.24 (A24), J4.24 (A24), J5.24 (A24), J6.24 (A24), J7.47 (Pin_47)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
- net SPARE renamed USR1
- net ~{VMA} renamed ~{ROM_{cs}}
- new net: R2.2, R4.1, SW1.1, SW1.3
- new net: C2.1, R4.2, U1.1
- new net: C1.1, R1.2, U1.3
- new net: U1.4, U1.5
- new net: U1.6, U2.4 (~{S})
- new net: U1.2, U2.3 (C)
- new net: U2.2 (D), U2.6 (~{Q})
- new net: R3.1, SW1.6 (A)
- new net CLK1: J1.18 (B9), J10.18 (B9), J11.18 (B9), J12.18 (B9), J13.18 (B9), J14.18 (B9), J2.18 (B9), J3.18 (B9), J4.18 (B9), J5.18 (B9), J6.18 (B9), J7.18 (Pin_18)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
- new net CLK2: J1.20 (B10), J10.20 (B10), J11.20 (B10), J12.20 (B10), J13.20 (B10), J14.20 (B10), J2.20 (B10), J3.20 (B10), J4.20 (B10), J5.20 (B10), J6.20 (B10), J7.20 (Pin_20)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
- new net RESET: J1.24 (B12), J10.24 (B12), J11.24 (B12), J12.24 (B12), J13.24 (B12), J14.24 (B12), J2.24 (B12), J3.24 (B12), J4.24 (B12), J5.24 (B12), J6.24 (B12), J7.24 (Pin_24)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
- new net USR2: J1.56 (B28), J10.56 (B28), J11.56 (B28), J12.56 (B28), J13.56 (B28), J14.56 (B28), J2.56 (B28), J3.56 (B28), J4.56 (B28), J5.56 (B28), J6.56 (B28), J7.56 (Pin_56)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
- new net USR3: J1.58 (B29), J10.58 (B29), J11.58 (B29), J12.58 (B29), J13.58 (B29), J14.58 (B29), J2.58 (B29), J3.58 (B29), J4.58 (B29), J5.58 (B29), J6.58 (B29), J7.58 (Pin_58)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
- new net USR4: J1.60 (B30), J10.60 (B30), J11.60 (B30), J12.60 (B30), J13.60 (B30), J14.60 (B30), J2.60 (B30), J3.60 (B30), J4.60 (B30), J5.60 (B30), J6.60 (B30), J7.60 (Pin_60)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
- new net VCC: J8.9 (+5VSB), R1.1, R2.1, U1.11, U1.13, U1.14 (VCC), U1.9, U2.10 (~{S}), U2.11 (C), U2.12 (D), U2.13 (~{R}), U2.14 (VCC)
- new net ~{CART_{en}}: J1.16 (B8), J10.16 (B8), J11.16 (B8), J12.16 (B8), J13.16 (B8), J14.16 (B8), J2.16 (B8), J3.16 (B8), J4.16 (B8), J5.16 (B8), J6.16 (B8), J7.16 (Pin_16)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
- new net ~{MMU_{en}}: J1.39 (A20), J10.39 (A20), J11.39 (A20), J12.39 (A20), J13.39 (A20), J14.39 (A20), J2.39 (A20), J3.39 (A20), J4.39 (A20), J5.39 (A20), J6.39 (A20), J7.39 (Pin_39)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
- new net ~{PS_ON}: J8.16 (~{PS_ON}), U2.5 (Q)
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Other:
- removed sheet Power
- note added: "ATX POWER CONNECTOR"
- note added: "ATX POWER ON CIRCUIT"
- note added: "Basic switch debounce."
- note added: "ESD Protection (At ATX PSU connector level)"
- note added: "ESD Protection (At header pin connector level)"
- note added: "This is a basic active low Power-On-Reset with a small RC delay."
